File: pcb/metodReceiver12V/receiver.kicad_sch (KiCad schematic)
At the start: 18 parts, among them J1 Conn_01x05_Socket, J1 WAGO 2061-602, J2 har-flexicon 2,54 MSH-4, J4 Conn_01x05_Socket, J5 Conn_01x05_Socket, J6 Conn_01x05_Socket, U1 TLV76050, U2 ISL3280ExHZ, U3 TLV76050, U4 ISL3280ExHZ

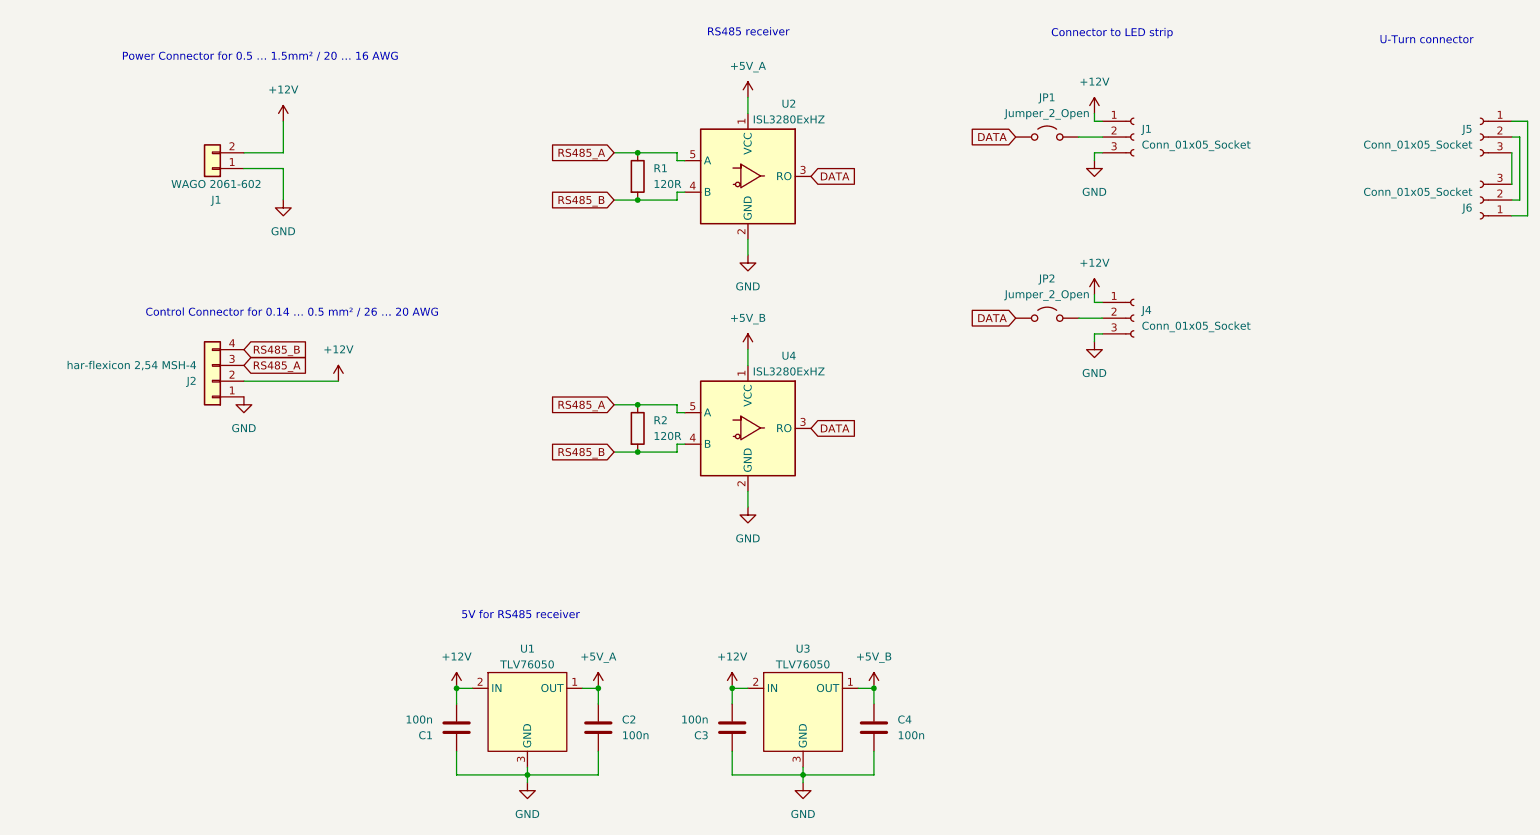
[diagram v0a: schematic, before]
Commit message: Use ISL3280E
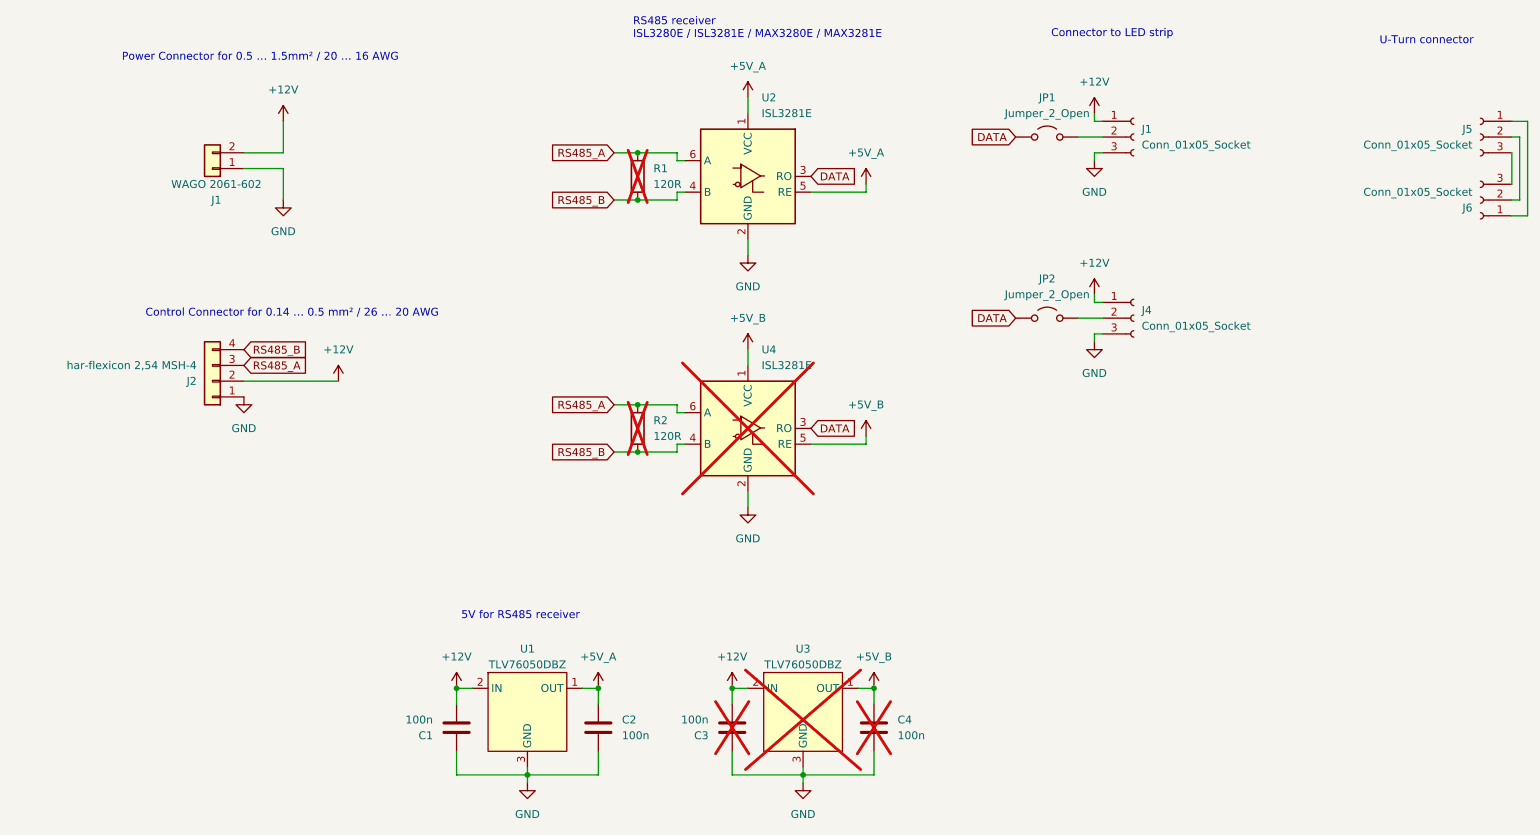
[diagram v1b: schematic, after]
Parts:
- removed U2, U4: ISL3280ExHZ, local:ISL3280E, symbol Interface_UART:ISL3280ExHZ
- added U2, U4: ISL3281E, local:ISL3281E, symbol Interface_UART:ISL3281ExHZ
- C1, C2: footprint Capacitor_SMD:C_0603_1608Metric -> local:0603
- C3, C4: footprint Capacitor_SMD:C_0603_1608Metric -> local:0603; now not fitted
- J1, J2, J4, J5, J6, JP1, JP2: now left out of the parts list
- R1, R2: footprint Resistor_SMD:R_1206_3216Metric -> local:1206; now not fitted
- U1: value TLV76050 -> TLV76050DBZ
- U3: value TLV76050 -> TLV76050DBZ; now not fitted
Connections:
- net +5V_A: now also U2.1 (VCC), U2.5 (RE)
- net +5V_B: now also U4.1 (VCC), U4.5 (RE)
- net DATA: now also U2.3 (RO), U4.3 (RO)
- net GND: now also U2.2 (GND), U4.2 (GND)
- net RS485_A: now also U2.6 (A), U4.6 (A)
- net RS485_B: now also U2.4 (B), U4.4 (B)
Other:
- note added: "RS485 receiver ISL3280E / ISL3281E / MAX3280E / MAX3281E"
- note removed: "RS485 receiver"
